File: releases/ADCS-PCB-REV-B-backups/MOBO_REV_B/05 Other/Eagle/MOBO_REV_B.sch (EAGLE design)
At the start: 139 parts, among them J1 HDR_10_EZFET_DEBUGGER, J3 832-10-012-10-005000, J5 CNC_3221-10-0300-00, J7 830-10-003-20-005000, J8 830-10-006-20-005000, Q1 BSR802NL6327HTSA1, U1 MSP430F5529IPN, U10 TSV991AILT, U2 TSV991AILT, U3 ADS7841E_2K5, U4 TSV991AILT, U5 DMC4050SSDQ-13, U6 BNO055, U7 HMC1053, U9 BMX160, Y1 32.768kHz, Y2 CSTCR4M00G15L99, Y3 32.768kHz

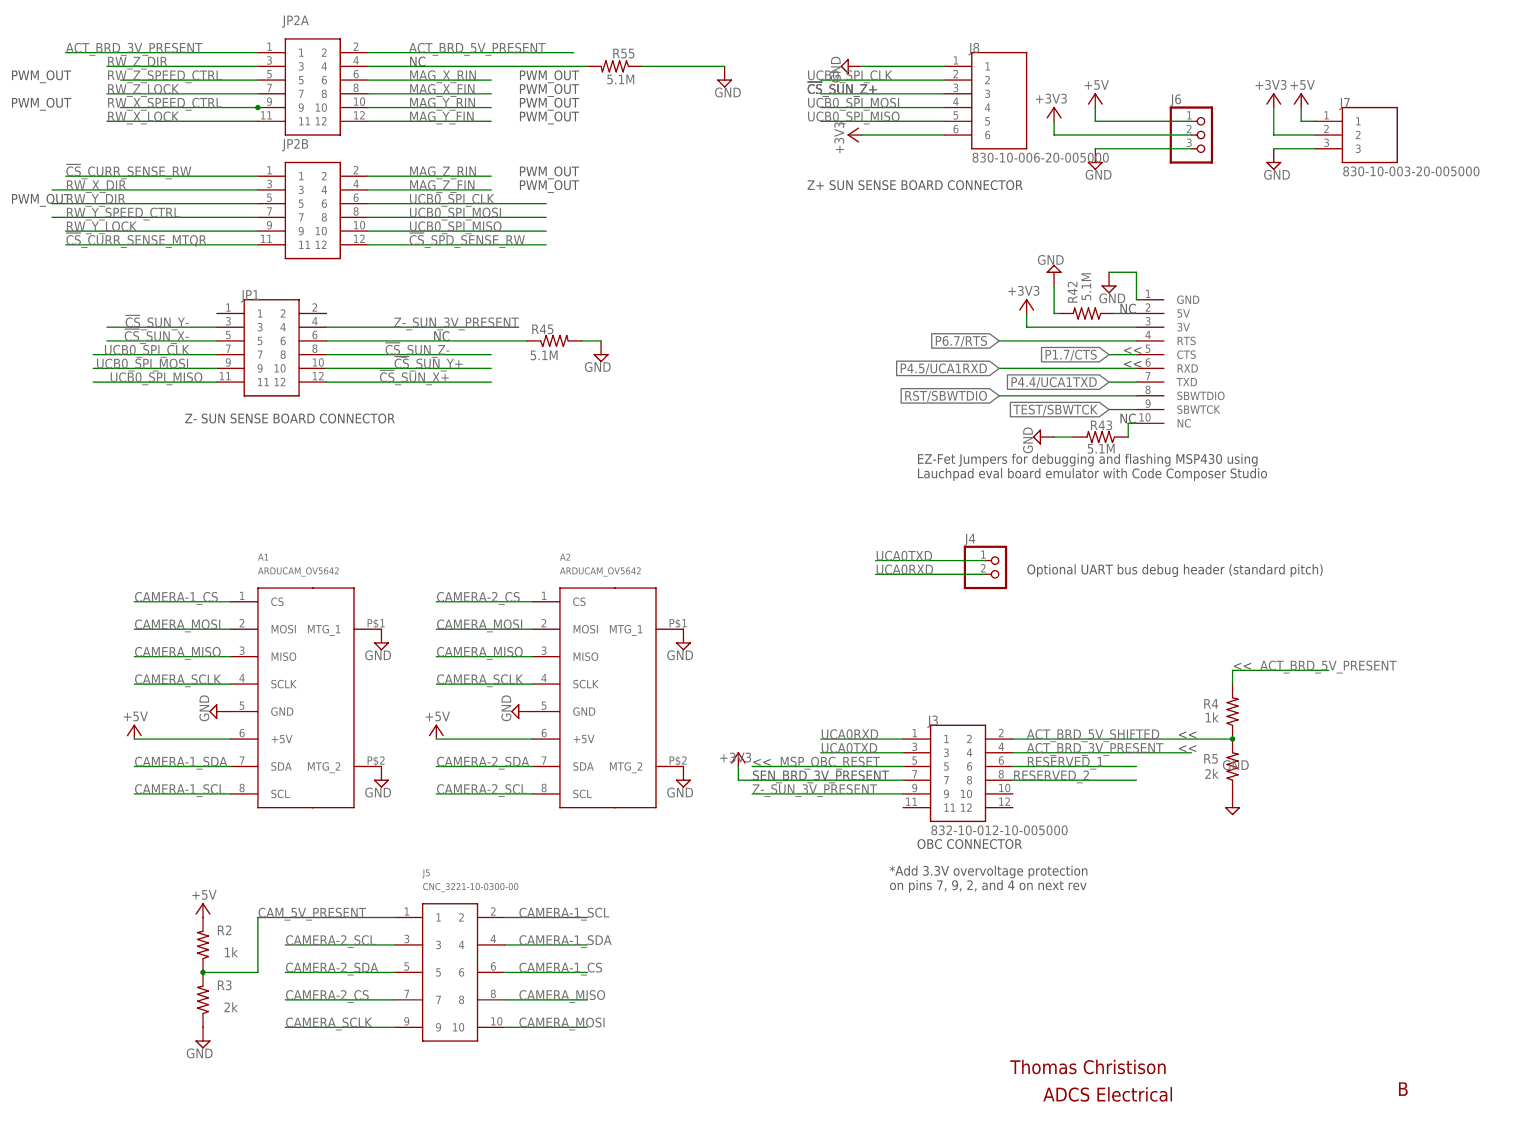
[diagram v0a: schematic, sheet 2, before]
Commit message: Finalized connectors for Luc and reattached burn wire
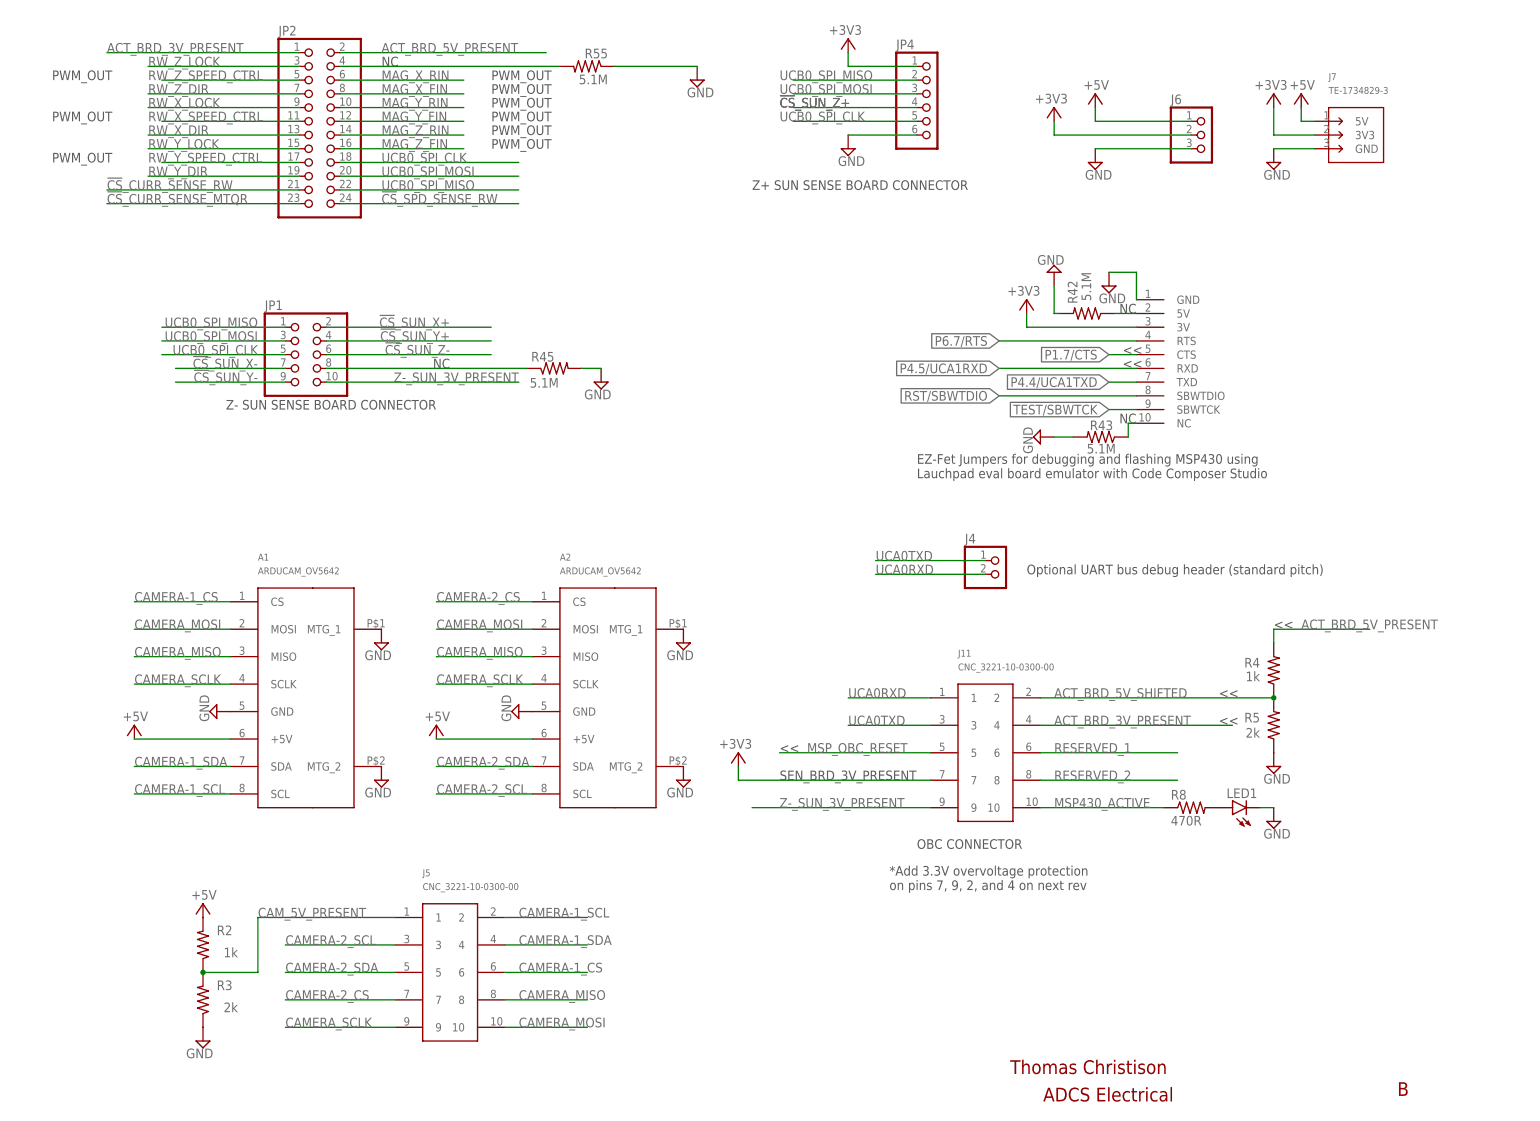
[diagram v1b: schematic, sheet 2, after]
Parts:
- removed J3, JP2A, JP2B: 832-10-012-10-005000, 832-10-012-10-005000:832-10-012-10-005000
- removed J8: 830-10-006-20-005000, 830-10-006-20-005000:830-10-006-20-005000
- added J11: CNC_3221-10-0300-00, my_library:CNC_3221-10-0300-00
- added JP2: (no value), pinhead:PINHD-2X12
- added JP4: (no value), my_library:PINHD-1X6
- added LED1, LED2, LED3: (no value), led:LEDCHIP-LED0603
- added R31, R8: 470R, rcl:R-US_R0603
- added R32: 750R, rcl:R-US_R0603
- J7: value 830-10-003-20-005000 -> TE-1734829-3; device 830-10-003-20-005000:830-10-003-20-005000 -> my_library:TE-1734829-3
- JP1: value 832-10-012-10-005000 -> (none); device 832-10-012-10-005000:832-10-012-10-005000 -> pinhead:PINHD-2X5
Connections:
- new net N$4: LED1.A, R8.2
- new net N$5: LED2.A, R31.2
- new net N$6: LED3.A, R32.2
- net !CS!_CURR_SENSE_MTQR: now also JP2.23; no longer JP2B.11
- net !CS!_CURR_SENSE_RW: now also JP2.21; no longer JP2B.1
- net !CS!_SPD_SENSE_RW: now also JP2.24; no longer JP2B.12
- net !CS!_SUN_X+: now also JP1.2; no longer JP1.12
- net !CS!_SUN_X-: now also JP1.7; no longer JP1.5
- net !CS!_SUN_Y+: now also JP1.4; no longer JP1.10
- net !CS!_SUN_Y-: now also JP1.9; no longer JP1.3
- net !CS!_SUN_Z+: now also JP4.4; no longer J8.3
- net !CS!_SUN_Z-: now also JP1.6; no longer JP1.8
- net +3V3: now also J11.7, J7.3V3, JP4.1, R31.1; no longer J3.7, J7.2, J8.6
- net +5V: now also J7.5V, R32.1; no longer J7.1
- net ACT_BRD_3V_PRESENT: now also J11.4, JP2.1; no longer J3.4, JP2A.1
- net ACT_BRD_5V_PRESENT: now also JP2.2; no longer JP2A.2
- net ACT_BRD_5V_SHIFTED: now also J11.2; no longer J3.2
- net GND: now also J7.GND, JP4.6, LED1.C, LED2.C, LED3.C; no longer J7.3, J8.1
- net MAG_X_FIN: now also JP2.8; no longer JP2A.8
- net MAG_X_RIN: now also JP2.6; no longer JP2A.6
- net MAG_Y_FIN: now also JP2.12; no longer JP2A.12
- net MAG_Y_RIN: now also JP2.10; no longer JP2A.10
- net MAG_Z_FIN: now also JP2.16; no longer JP2B.4
- net MAG_Z_RIN: now also JP2.14; no longer JP2B.2
- net MSP430_ACTIVE: now also J11.10, R8.1
- net MSP_OBC_RESET: now also J11.5; no longer J3.5
- net N$1: now also JP2.4; no longer JP2A.4
- net N$58: now also JP1.8; no longer JP1.6
- net RESERVED_1: now also J11.6; no longer J3.6
- net RESERVED_2: now also J11.8; no longer J3.8
- net RW_X_DIR: now also JP2.13; no longer JP2B.3
- net RW_X_LOCK: now also JP2.9; no longer JP2A.11
- net RW_X_SPEED_CTRL: now also JP2.11; no longer JP2A.9
- net RW_Y_DIR: now also JP2.19; no longer JP2B.5
- net RW_Y_LOCK: now also JP2.15; no longer JP2B.9
- net RW_Y_SPEED_CTRL: now also JP2.17; no longer JP2B.7
- net RW_Z_DIR: now also JP2.7; no longer JP2A.3
- net RW_Z_LOCK: now also JP2.3; no longer JP2A.7
- net RW_Z_SPEED_CTRL: now also JP2.5; no longer JP2A.5
- net UCA0RXD: now also J11.1; no longer J3.1
- net UCA0TXD: now also J11.3; no longer J3.3
- net UCB0_SPI_CLK: now also JP1.5, JP2.18, JP4.5; no longer J8.2, JP1.7, JP2B.6
- net UCB0_SPI_MISO: now also JP1.1, JP2.22, JP4.2; no longer J8.5, JP1.11, JP2B.10
- net UCB0_SPI_MOSI: now also JP1.3, JP2.20, JP4.3; no longer J8.4, JP1.9, JP2B.8
- net Z-_SUN_3V_PRESENT: now also J11.9, JP1.10; no longer J3.9, JP1.4
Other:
- moved on the sheet: R4, R45, R5, R55
